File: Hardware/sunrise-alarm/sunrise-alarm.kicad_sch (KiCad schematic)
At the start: 38 parts

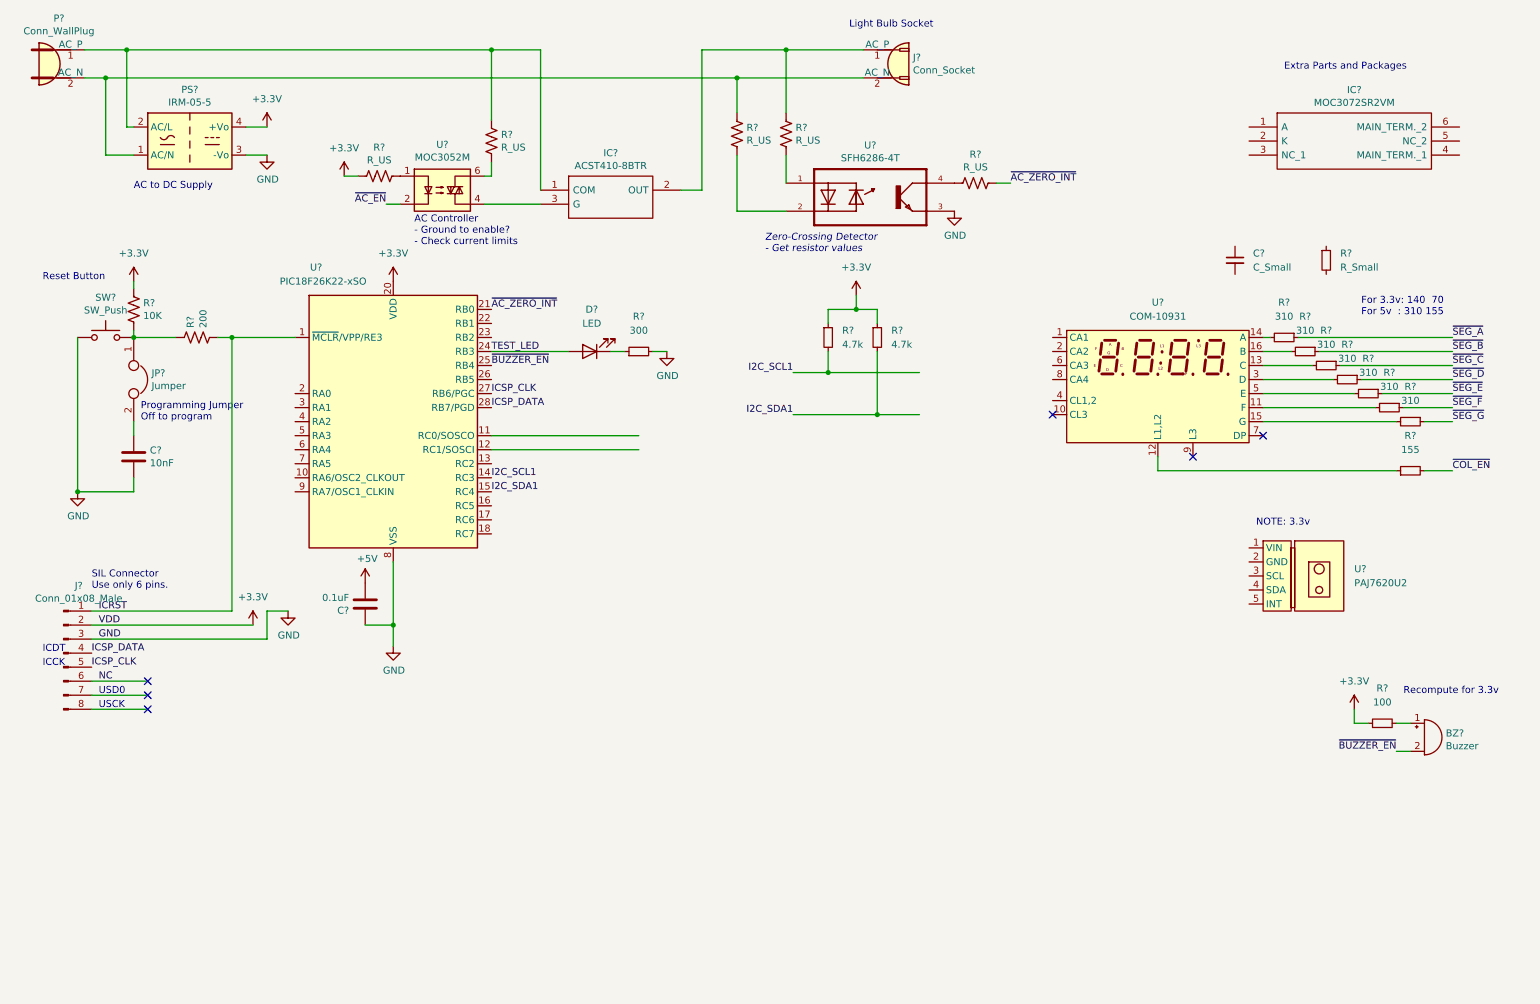
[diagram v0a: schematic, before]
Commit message: hw: Schematic v4. Pin Assignments
Schematic for LED Display.
*Noticed LED Display needs 5v!*
Add PIN assignments.
Added PIN assignments for gesture sensor.
Moved Schematic to hardware folder.
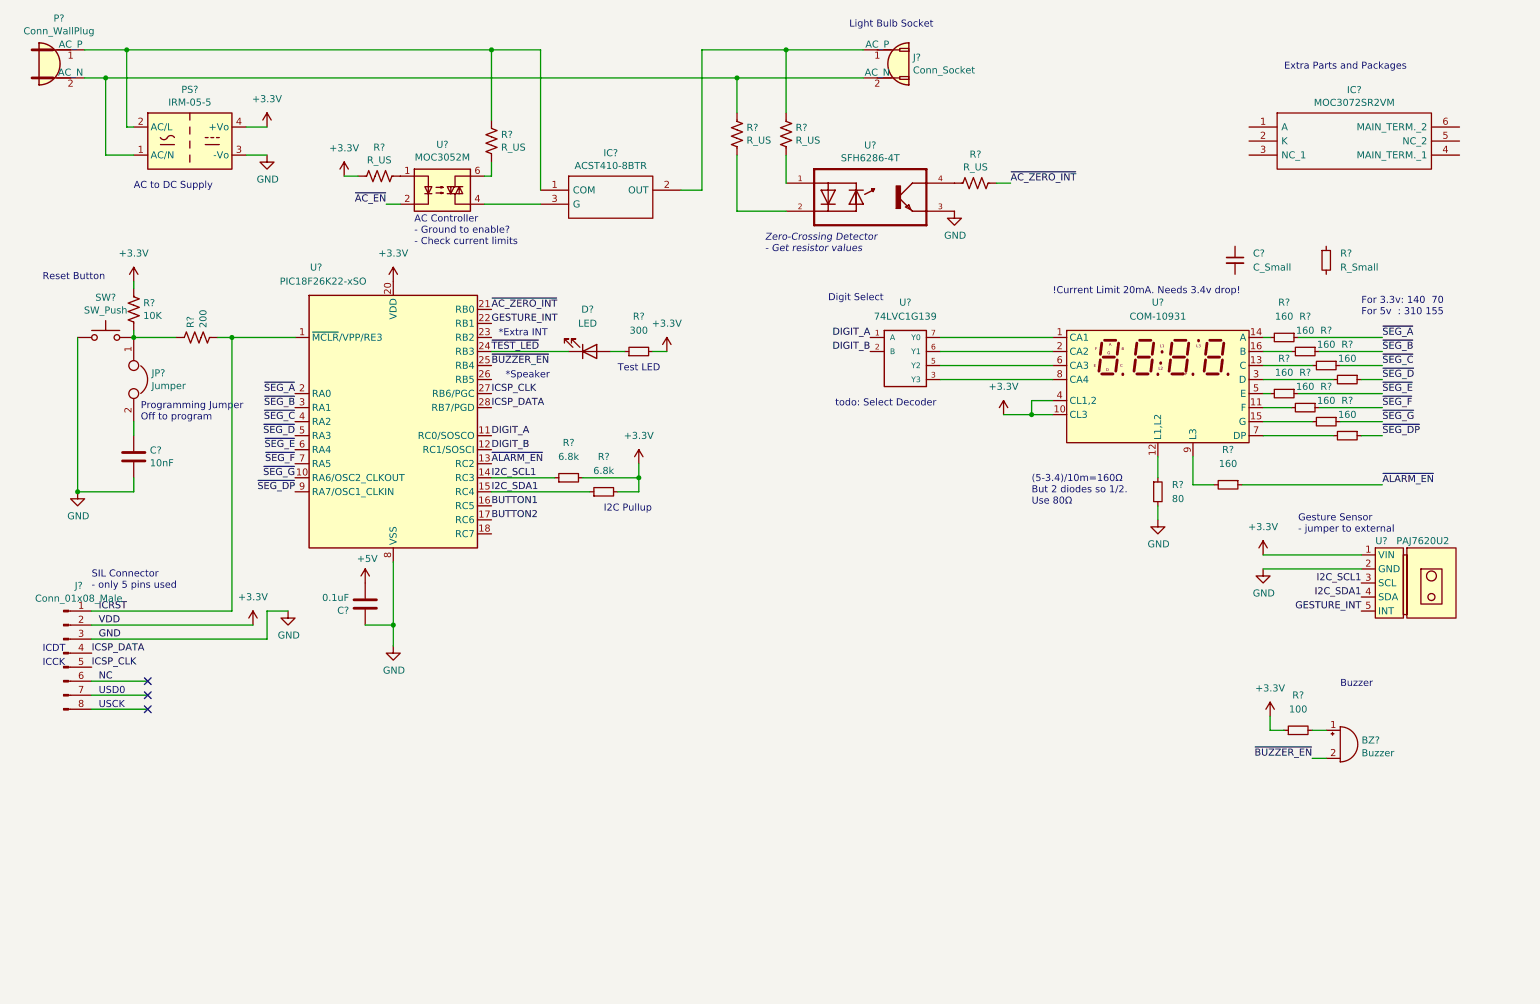
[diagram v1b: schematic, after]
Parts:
- removed R? (x2): 4.7k, symbol Device:R_Small
- added R? (x2): 160, symbol Device:R_Small
- added R? (x2): 6.8k, symbol Device:R_Small
- added U?: 74LVC1G139, symbol 74xGxx:74LVC1G139
- R?: value 155 -> 80
- R? (x7): value 310 -> 160
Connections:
- net ~{COL_EN} is gone; now on net GND: R?.2
- net +3V3: now also R?.2, U?.1 (VIN), U?.10 (CL3), U?.4 (CL1,2), R?.2, R?.2
- net GND: now also U?.2 (GND), U?.4 (GND); no longer R?.2
- net I2C_SCL1: now also U?.3 (SCL), R?.1
- net I2C_SDA1: now also U?.4 (SDA), R?.1
- net ~{SEG_A}: now also U?.2 (RA0)
- net ~{SEG_B}: now also U?.3 (RA1)
- net ~{SEG_C}: now also U?.4 (RA2)
- net ~{SEG_D}: now also U?.5 (RA3)
- net ~{SEG_E}: now also U?.6 (RA4)
- net ~{SEG_F}: now also U?.7 (RA5)
- net ~{SEG_G}: now also U?.10 (RA6/OSC2_CLKOUT)
- net DIGIT_A: now reaches U?.11 (RC0/SOSCO)
- net DIGIT_A: now also U?.1 (A)
- net DIGIT_B: now reaches U?.12 (RC1/SOSCI)
- net DIGIT_B: now also U?.2 (B)
- net ~{ALARM_EN}: now reaches U?.13 (RC2)
- net ~{ALARM_EN}: now also R?.1
- net BUTTON1: now reaches U?.16 (RC5)
- net BUTTON2: now reaches U?.17 (RC6)
- net GESTURE_INT: now reaches U?.22 (RB1)
- net GESTURE_INT: now also U?.5 (INT)
- net ~{SEG_DP}: now reaches U?.9 (RA7/OSC1_CLKIN)
- net ~{SEG_DP}: now also R?.1
- net at R?.1: now also D?.2 (A); no longer D?.1 (K)
- net at U?.1 (CA1): now also U?.7 (Y0)
- net at U?.2 (CA2): now also U?.6 (Y1)
- net at U?.6 (CA3): now also U?.5 (Y2)
- net at U?.7 (DP): now also R?.2
- net at U?.8 (CA4): now also U?.3 (Y3)
- net at U?.9 (L3): now also R?.2
- net TEST_LED renamed ~{TEST_LED}
- net ~{TEST_LED}: now also D?.1 (K); no longer D?.2 (A)
- new net VCC: U?.8 (VCC)
- no-connect marks 6 -> 3
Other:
- note added: "!Current Limit 20mA. Needs 3.4v drop!"
- note added: "(5-3.4)/10m=160Ω But 2 diodes so 1/2. Use 80Ω"
- note added: "*Extra INT"
- note added: "*Speaker"
- note added: "Buzzer"
- note added: "Digit Select"
- note added: "Gesture Sensor - jumper to external"
- note added: "I2C Pullup"
- note added: "SIL Connector - only 5 pins used"
- note added: "Test LED"
- note added: "todo: Select Decoder"
- note removed: "NOTE: 3.3v"
- note removed: "Recompute for 3.3v"
- note removed: "SIL Connector Use only 6 pins."
- moved on the sheet: BZ?, D?, R?, U?

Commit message: hw: Added Complete schematic v0.5 + datasheets
- Updated 5v to 3.3v Power Supply.
- Updated Logic control for LED Display.
  Use single decoder with V_IH = 1.5v. Works for 1-way control.
- Added a third digit line for alarm and colon.
- Finished buzzer circuit. Tested prototype.
- Corrected Zero Crossing Circuit to be on power line always.
- Corrected Triac Driver resistor to feedback from OUT of power triac.
- Updated symbols.
- AC System Done!
- Added Jumper to Gesture Sensor.
- Tested: Display Works fine with 3.3v. Use Either.
- Added Oscillator
- Added Varistor
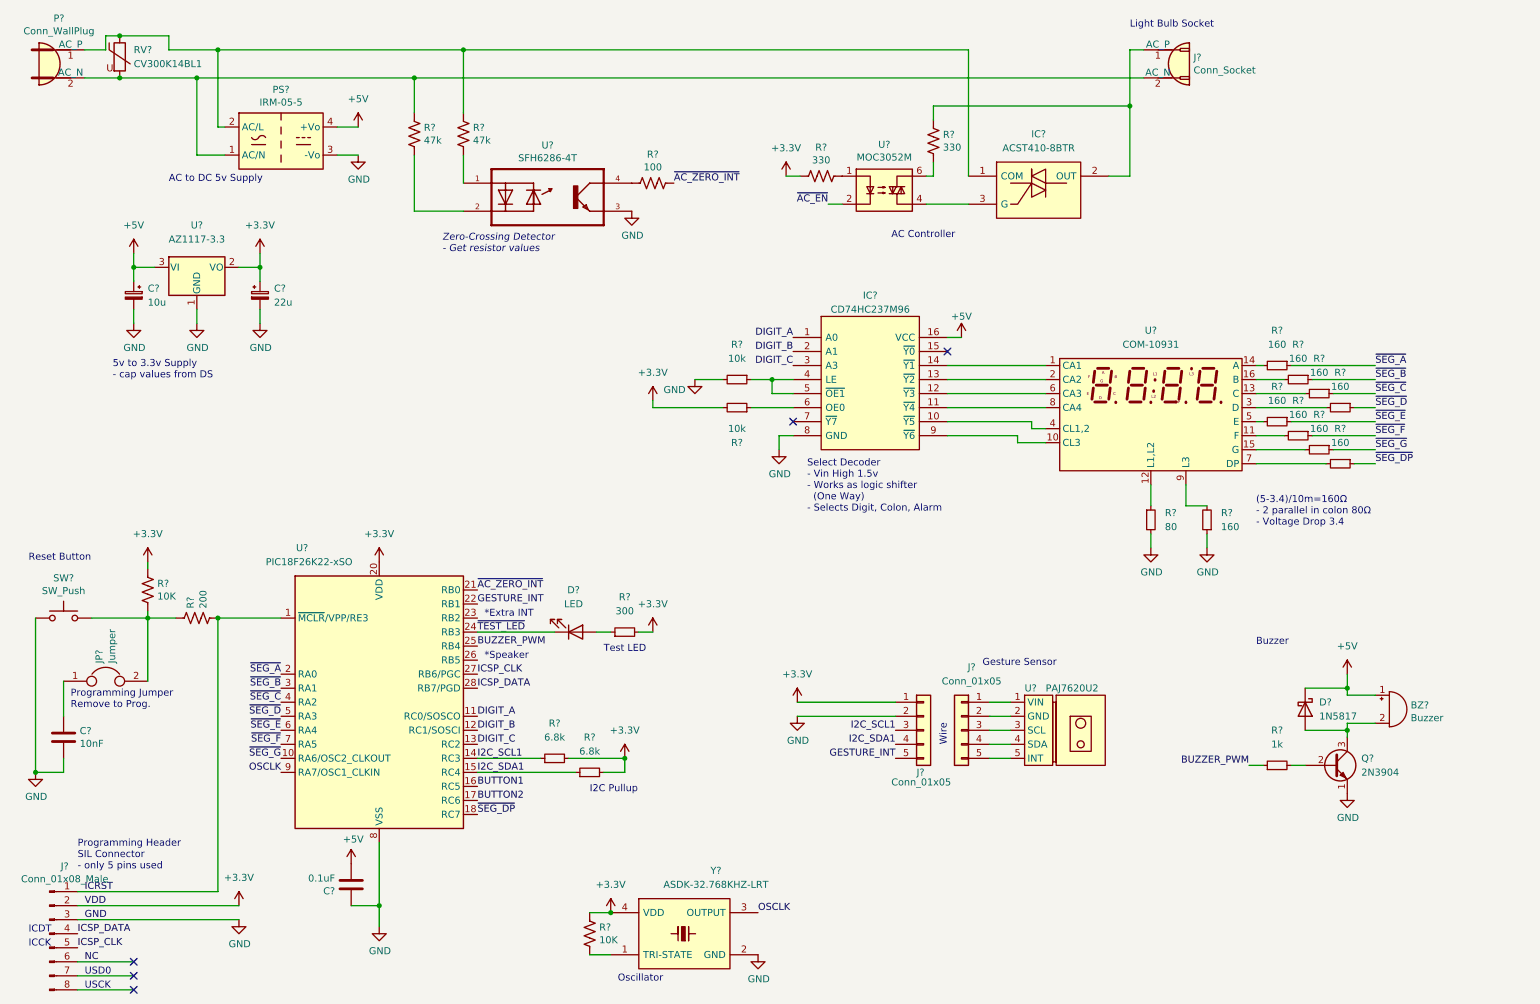
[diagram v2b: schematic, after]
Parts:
- removed C?: C_Small, symbol Device:C_Small
- removed IC?: MOC3072SR2VM, SOP254P916X480-6N, symbol SamacSys_Parts:MOC3072SR2VM
- removed IC?: ACST410-8BTR, ACST4108BTR, symbol SamacSys_Parts:ACST410-8BTR
- removed R?: R_Small, symbol Device:R_Small
- removed U?: 74LVC1G139, symbol 74xGxx:74LVC1G139
- added C?: 10u, symbol Device:C_Polarized_Small
- added C?: 22u, symbol Device:C_Polarized_Small
- added D?: 1N5817, Diode_THT:D_DO-41_SOD81_P10.16mm_Horizontal, symbol Diode:1N5817
- added IC?: ACST410-8BTR, ACST4108BTR, symbol Custom:ACST410-8BTR
- added IC?: CD74HC237M96, SOIC127P600X175-16N, symbol SamacSys_Parts:CD74HC237M96
- added J? (x2): Conn_01x05, Connector_Harwin:Harwin_M20-89005xx_1x05_P2.54mm_Horizontal, symbol Connector_Generic:Conn_01x05
- added Q?: 2N3904, Package_TO_SOT_THT:TO-92, symbol Transistor_BJT:2N3904
- added R? (x2): 10k, symbol Device:R_Small
- added R?: 10K, symbol Device:R_US
- added RV?: CV300K14BL1, symbol Device:Varistor
- added U?: AZ1117-3.3, Package_TO_SOT_SMD:SOT-89-3_Handsoldering, symbol Regulator_Linear:AZ1117-3.3
- added Y?: ASDK-32.768KHZ-LRT, ASDK32768KHZLRT, symbol SamacSys_Parts:ASDK-32.768KHZ-LRT
- R? (x2): value R_US -> 330
- R? (x2): value R_US -> 47k
- R?: value R_US -> 100
- R?: value 100 -> 1k
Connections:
- net +3V3: now also C?.1, J?.1 (Pin_1), R?.1, R?.2, U?.2 (VO), Y?.4 (VDD); no longer PS?.4 (+Vo), R?.1, U?.1 (VIN), U?.10 (CL3), U?.4 (CL1,2)
- net DIGIT_A: now also IC?.1 (A0)
- net DIGIT_B: now also IC?.2 (A1)
- net GESTURE_INT: now also J?.5 (Pin_5); no longer U?.5 (INT)
- net GND: now also R?.1, C?.2, C?.2, IC?.8 (GND), J?.2 (Pin_2), Q?.1 (E), R?.2, U?.1 (GND), Y?.2 (GND); no longer U?.2 (GND)
- net I2C_SCL1: now also J?.3 (Pin_3); no longer U?.3 (SCL)
- net I2C_SDA1: now also J?.4 (Pin_4); no longer U?.4 (SDA)
- net ~{SEG_DP}: now also U?.18 (RC7); no longer U?.9 (RA7/OSC1_CLKIN)
- net at J?.2 (AC_N), P?.2 (AC_N), PS?.1 (AC/N)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: now also RV?.2
- net at P?.1 (AC_P), PS?.2 (AC/L): now also R?.1, IC?.1 (COM), RV?.1; no longer R?.1
- net at U?.4: now also IC?.3 (G)
- net at J?.1 (AC_P): now also R?.1, IC?.2 (OUT); no longer R?.1
- net at R?.1, R?.2, SW?.2: now also JP?.2; no longer JP?.1
- net at R?.2: now also Q?.2 (B); no longer BZ?.1 (-)
- net at C?.1: now also JP?.1; no longer JP?.2
- net at U?.1 (CA1): now also IC?.14 (~{Y1})
- net at U?.2 (CA2): now also IC?.13 (~{Y2})
- net at U?.6 (CA3): now also IC?.12 (~{Y3})
- net at U?.8 (CA4): now also IC?.11 (~{Y4})
- net ~{ALARM_EN} renamed DIGIT_C
- net DIGIT_C: now also IC?.3 (A3); no longer R?.1
- net ~{BUZZER_EN}: no longer names the net of BZ?.2 (+)
- net ~{BUZZER_EN}: now also D?.2 (A), Q?.3 (C); no longer U?.25 (RB4)
- new net: IC?.4 (LE), IC?.5 (~{OE1}), R?.1
- new net: J?.1 (Pin_1), U?.1 (VIN)
- new net: J?.2 (Pin_2), U?.2 (GND)
- new net: J?.3 (Pin_3), U?.3 (SCL)
- new net: J?.4 (Pin_4), U?.4 (SDA)
- new net: J?.5 (Pin_5), U?.5 (INT)
- new net: IC?.9 (~{Y6}), U?.10 (CL3)
- new net: IC?.10 (~{Y5}), U?.4 (CL1,2)
- new net: R?.2, Y?.1 (TRI-STATE)
- new net: IC?.6 (OE0), R?.1
- new net +5V: BZ?.1 (-), C?.1, D?.1 (K), IC?.16 (VCC), PS?.4 (+Vo), U?.3 (VI)
- new net BUZZER_PWM: R?.1, U?.25 (RB4)
- new net OSCLK: U?.9 (RA7/OSC1_CLKIN), Y?.3 (OUTPUT)
- no-connect marks 3 -> 5
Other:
- note added: "(5-3.4)/10m=160Ω - 2 parallel in colon 80Ω - Voltage Drop 3.4"
- note added: "5v to 3.3v Supply - cap values from DS"
- note added: "AC Controller"
- note added: "AC to DC 5v Supply"
- note added: "Gesture Sensor"
- note added: "Oscillator"
- note added: "Programming Header SIL Connector - only 5 pins used"
- note added: "Programming Jumper Remove to Prog."
- note added: "Select Decoder - Vin High 1.5v - Works as logic shifter (One Way) - Selects Digit, Colon, Alarm"
- note added: "Wire"
- note removed: "!Current Limit 20mA. Needs 3.4v drop!"
- note removed: "(5-3.4)/10m=160Ω But 2 diodes so 1/2. Use 80Ω"
- note removed: "AC Controller - Ground to enable? - Check current limits"
- note removed: "AC to DC Supply"
- note removed: "Digit Select"
- note removed: "Extra Parts and Packages"
- note removed: "For 3.3v: 140 70 For 5v : 310 155"
- note removed: "Gesture Sensor - jumper to external"
- note removed: "Programming Jumper Off to program"
- note removed: "SIL Connector - only 5 pins used"
- note removed: "todo: Select Decoder"
- moved on the sheet: BZ?, C?, D?, J?, JP?, PS?, R?, SW?, U?

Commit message: Updated Schematic Buttons, Connector, Ran ERC
- Added buttons.
- Added AC to Main board connection. Split power lines.
- Corrected non-connected.
- Updated schematic symbols.
- Ran annotations. Components now have numbers.
- Ran ERC check.
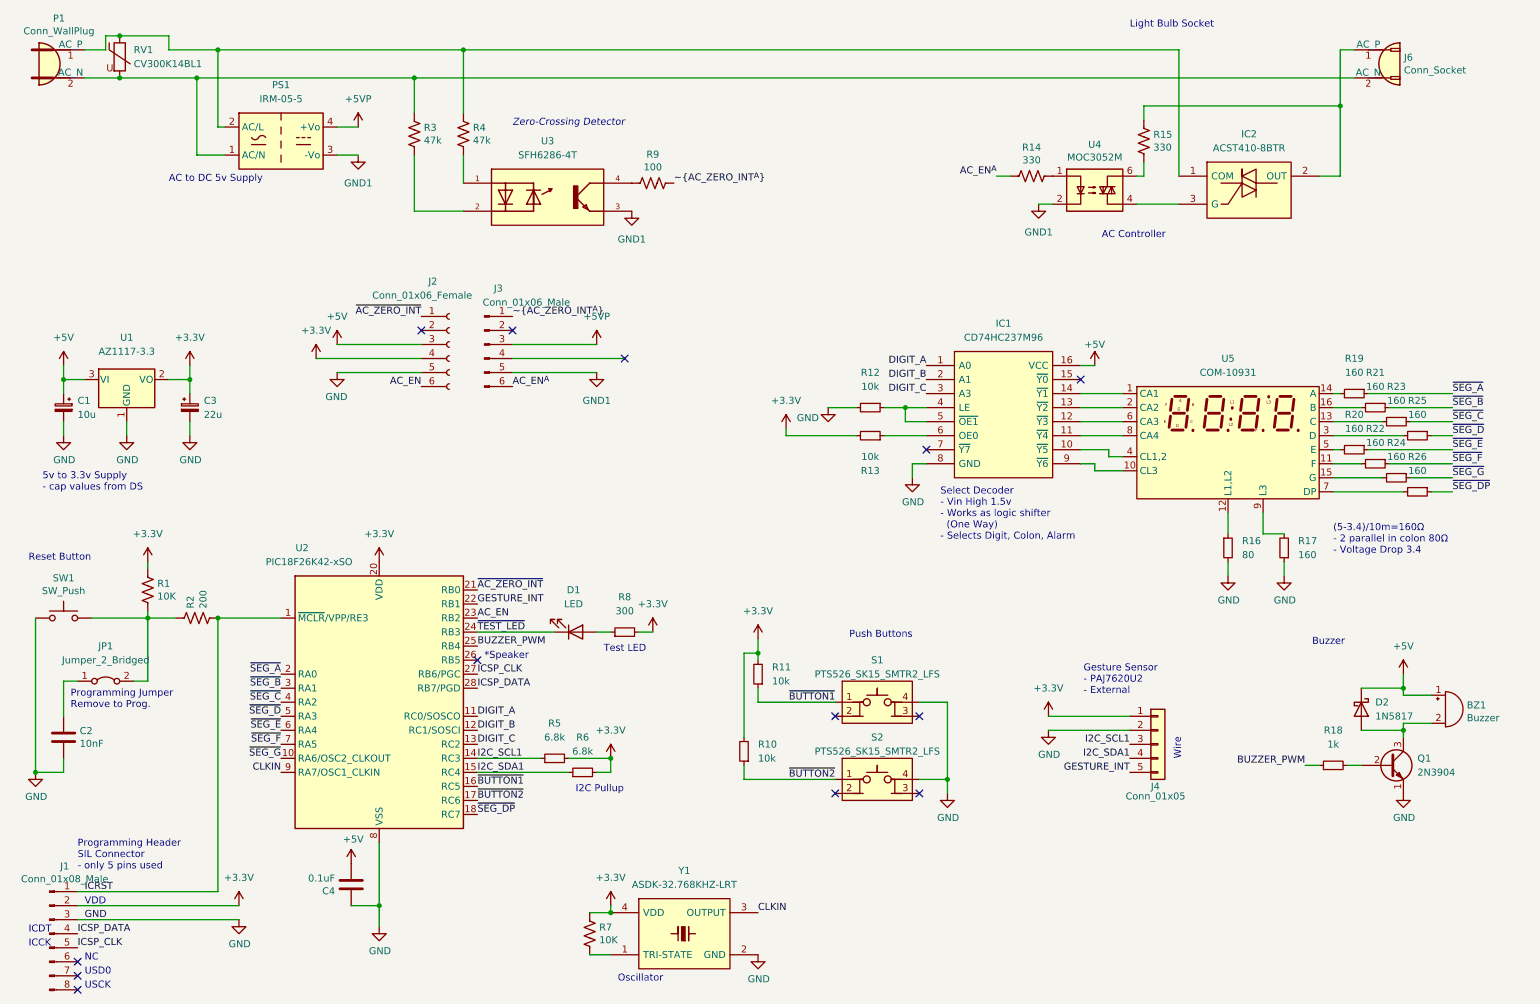
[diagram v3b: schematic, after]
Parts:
- removed J?: Conn_01x05, Connector_Harwin:Harwin_M20-89005xx_1x05_P2.54mm_Horizontal, symbol Connector_Generic:Conn_01x05
- removed JP?: Jumper, symbol Device:Jumper
- removed PS?: IRM-05-5, Converter_ACDC:Converter_ACDC_MeanWell_IRM-05-xx_THT, symbol Converter_ACDC:IRM-05-3.3
- removed U?: SFH6286-4T, SOIC254P977X460-4N, symbol SFH6286-4T:SFH6286-4T
- removed U?: PAJ7620U2, symbol Custom:PAJ7620U2
- removed Y?: ASDK-32.768KHZ-LRT, ASDK32768KHZLRT, symbol SamacSys_Parts:ASDK-32.768KHZ-LRT
- added J2: Conn_01x06_Female, symbol Connector:Conn_01x06_Female
- added J3: Conn_01x06_Male, symbol Connector:Conn_01x06_Male
- added JP1: Jumper_2_Bridged, TestPoint:TestPoint_2Pads_Pitch2.54mm_Drill0.8mm, symbol Jumper:Jumper_2_Bridged
- added PS1: IRM-05-5, Converter_ACDC:Converter_ACDC_MeanWell_IRM-05-xx_THT, symbol Converter_ACDC:IRM-05-5
- added R10, R11: 10k, symbol Device:R_Small
- added S1, S2: PTS526_SK15_SMTR2_LFS, PTS526SK15SMTR2LFS, symbol Custom:PTS526_SK15_SMTR2_LFS
- added U3: SFH6286-4T, SOIC254P977X460-4N, symbol Custom:SFH6286-4T
- added Y1: ASDK-32.768KHZ-LRT, ASDK32768KHZLRT, symbol Custom:ASDK-32.768KHZ-LRT
- U2: renamed from U?; value PIC18F26K22-xSO -> PIC18F26K42-xSO
- gave numbers to parts that had none: 43
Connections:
- net +3V3: now also J2.4 (Pin_4), R10.2, R11.2, Y1.4 (VDD); no longer R14.2
- net +5V: now also J2.3 (Pin_3)
- net GND: now also J2.5 (Pin_5), S1.4, S2.4, Y1.2 (GND)
- net ~{AC_ZERO_INT}: now also J2.1 (Pin_1); no longer R9.1
- net AC_EN: now reaches U2.23 (RB2)
- net AC_EN: now also J2.6 (Pin_6)
- net at J6.2 (AC_N), P1.2 (AC_N), R3.1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: now also PS1.1 (AC/N)
- net at IC2.1 (COM), P1.1 (AC_P), R4.1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: now also PS1.2 (AC/L)
- net at R1.2, R2.1, SW1.2: now also JP1.2 (B)
- net at R4.2: now also U3.1
- net at R3.2: now also U3.2
- net at R9.2: now also U3.4
- net at C2.1: now also JP1.1 (A)
- net at R7.2: now also Y1.1 (TRI-STATE)
- net BUTTON1 renamed ~{BUTTON1}
- net ~{BUTTON1}: now also R11.1, S1.1
- net BUTTON2 renamed ~{BUTTON2}
- net ~{BUTTON2}: now also R10.1, S2.1
- net NC: no longer names the net of J1.6 (Pin_6)
- net OSCLK renamed CLKIN
- net CLKIN: now also Y1.3 (OUTPUT)
- net ~{AC_EN} renamed GND1
- net GND1: now also J3.5 (Pin_5), PS1.3 (-Vo), U3.3
- new net +5VP: J3.3 (Pin_3), PS1.4 (+Vo)
- new net AC_EN^{A}: J3.6 (Pin_6), R14.2
- new net ~{AC_ZERO_INT^{A}}: J3.1 (Pin_1), R9.1
- no-connect marks 5 -> 13
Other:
- note added: "Gesture Sensor - PAJ7620U2 - External"
- note added: "NC"
- note added: "Push Buttons"
- note added: "VDD"
- note added: "Zero-Crossing Detector"
- note removed: "*Extra INT"
- note removed: "Gesture Sensor"
- note removed: "Zero-Crossing Detector - Get resistor values"
- moved on the sheet: BZ1, C1, C3, D2, IC1, IC2, J4, J6, Q1, R12, R13, R14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
